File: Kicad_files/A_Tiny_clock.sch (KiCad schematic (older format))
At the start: 29 parts, among them J1 Conn_01x03_Male, J2 USB_B, Q1 Q_NPN_CBE, Q2 Q_NPN_CBE, SW1 SW_MEC_5E, SW2 SW_MEC_5E, SW3 SW_MEC_5E, SW4 SW_MEC_5E, SW5 SW_MEC_5E, U1 ATtiny13A-PU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

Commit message: Updated schematic
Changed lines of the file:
@@
 Text GLabel 6150 3650 2    50   Input ~ 0
 CLOCK_PIN
-$Comp
-L 74xx:74HC595 U3
-U 1 1 61E666FC
-P 8400 5450
-F 0 "U3" H 8400 4569 50  0000 C CNN
-F 1 "74HC595" H 8400 4660 50  0000 C CNN
-F 2 "" H 8400 5450 50  0001 C CNN
-F 3 "http://www.ti.com/lit/ds/symlink/sn74hc595.pdf" H 8400 5450 50  0001 C CNN
-	1    8400 5450
-	1    0    0    1
-$EndComp
 Text GLabel 8000 5850 0    50   Input ~ 0
 DATA_PIN
@@
 	1    7950 5250
 	0    1    1    0
-$EndComp
-Wire Wire Line
-	8800 4300 8000 4300
-Wire Wire Line
-	8000 4300 8000 4000
-$Comp
-L power:VCC #PWR0110
-U 1 1 61E6D320
-P 8400 6200
-F 0 "#PWR0110" H 8400 6050 50  0001 C CNN
-F 1 "VCC" H 8415 6373 50  0000 C CNN
-F 2 "" H 8400 6200 50  0001 C CNN
-F 3 "" H 8400 6200 50  0001 C CNN
-	1    8400 6200
-	-1   0    0    1
-$EndComp
-$Comp
-L power:VCC #PWR0111
-U 1 1 61E6D739
-P 8550 4200
-F 0 "#PWR0111" H 8550 4050 50  0001 C CNN
-F 1 "VCC" H 8565 4373 50  0000 C CNN
-F 2 "" H 8550 4200 50  0001 C CNN
-F 3 "" H 8550 4200 50  0001 C CNN
-	1    8550 4200
-	1    0    0    -1
 $EndComp
 $Comp
@@
 Text GLabel 8800 3800 2    50   Input ~ 0
 Dots
-$Comp
-L power:GND #PWR0116
-U 1 1 61EF6FD2
-P 8700 4750
-F 0 "#PWR0116" H 8700 4500 50  0001 C CNN
-F 1 "GND" H 8705 4577 50  0000 C CNN
-F 2 "" H 8700 4750 50  0001 C CNN
-F 3 "" H 8700 4750 50  0001 C CNN
-	1    8700 4750
-	-1   0    0    1
-$EndComp
 Wire Notes Line
 	4800 5250 500  5250
@@
 Wire Wire Line
 	5550 2900 5550 2950
-Wire Wire Line
-	8700 4750 8400 4750
-Wire Wire Line
-	8800 4300 8800 4950
+$Comp
+L power:GND #PWR0115
+U 1 1 61EF67DF
+P 8750 2750
+F 0 "#PWR0115" H 8750 2500 50  0001 C CNN
+F 1 "GND" H 8755 2577 50  0000 C CNN
+F 2 "" H 8750 2750 50  0001 C CNN
+F 3 "" H 8750 2750 50  0001 C CNN
+	1    8750 2750
+	1    0    0    -1
+$EndComp
+Wire Wire Line
+	8750 2750 8400 2900
+$Comp
+L Connector:Conn_01x03_Male J1
+U 1 1 6224BC17
+P 5700 2000
+F 0 "J1" H 5672 1932 50  0000 R CNN
+F 1 "Conn_01x03_Male" H 5672 2023 50  0000 R CNN
+F 2 "" H 5700 2000 50  0001 C CNN
+F 3 "~" H 5700 2000 50  0001 C CNN
+	1    5700 2000
+	-1   0    0    1
+$EndComp
+Text GLabel 5500 1900 0    50   Input ~ 0
+Clock_VCC
+Text GLabel 5500 2100 0    50   Input ~ 0
+Clock_GND
+Text GLabel 5500 2000 0    50   Input ~ 0
+Clock_Output
+Wire Wire Line
+	5550 4200 5550 4150
+$Comp
+L Connector:USB_B J2
+U 1 1 6226EF95
+P 2750 3800
+F 0 "J2" H 2807 4267 50  0000 C CNN
+F 1 "USB_B" H 2807 4176 50  0000 C CNN
+F 2 "" H 2900 3750 50  0001 C CNN
+F 3 " ~" H 2900 3750 50  0001 C CNN
+	1    2750 3800
+	1    0    0    -1
+$EndComp
+NoConn ~ 3050 3800
+NoConn ~ 3050 3900
+NoConn ~ 2650 4200
+$Comp
+L power:GND #PWR0117
+U 1 1 622821E8
+P 2750 4200
+F 0 "#PWR0117" H 2750 3950 50  0001 C CNN
+F 1 "GND" H 2755 4027 50  0000 C CNN
+F 2 "" H 2750 4200 50  0001 C CNN
+F 3 "" H 2750 4200 50  0001 C CNN
+	1    2750 4200
+	1    0    0    -1
+$EndComp
+$Comp
+L power:VCC #PWR0118
+U 1 1 62282B47
+P 3050 3600
+F 0 "#PWR0118" H 3050 3450 50  0001 C CNN
+F 1 "VCC" H 3065 3773 50  0000 C CNN
+F 2 "" H 3050 3600 50  0001 C CNN
+F 3 "" H 3050 3600 50  0001 C CNN
+	1    3050 3600
+	1    0    0    -1
+$EndComp
+Text Notes 700  3200 0    50   ~ 0
+I soldered wire (with male USB A plug on the other side of wire) directly to board.  \nHere on shcematic i power input is represented by USB B conector but it can be any 5V power supply.
+Wire Notes Line
+	650  4400 4400 4400
+Wire Notes Line
+	4400 4400 4400 3250
+Wire Notes Line
+	4400 3250 4800 3250
+Wire Notes Line
+	4800 3250 4800 3000
+Wire Notes Line
+	4800 3000 650  3000
+Wire Notes Line
+	650  3000 650  4400
+Connection ~ 9950 5950
+Wire Notes Line
+	7100 550  7100 3200
+Wire Notes Line
+	7100 3200 7500 3200
+Wire Notes Line
+	7500 3200 7500 3650
+Wire Notes Line
+	7500 3650 7100 3650
+Wire Notes Line
+	7100 3650 7100 6500
+$Comp
+L power:GND #PWR0116
+U 1 1 61EF6FD2
+P 8950 4750
+F 0 "#PWR0116" H 8950 4500 50  0001 C CNN
+F 1 "GND" H 8955 4577 50  0000 C CNN
+F 2 "" H 8950 4750 50  0001 C CNN
+F 3 "" H 8950 4750 50  0001 C CNN
+	1    8950 4750
+	1    0    0    -1
+$EndComp
+Wire Wire Line
+	8950 4750 8400 4750
+$Comp
+L power:VCC #PWR0110
+U 1 1 61E6D320
+P 8650 6200
+F 0 "#PWR0110" H 8650 6050 50  0001 C CNN
+F 1 "VCC" H 8665 6373 50  0000 C CNN
+F 2 "" H 8650 6200 50  0001 C CNN
+F 3 "" H 8650 6200 50  0001 C CNN
+	1    8650 6200
+	1    0    0    -1
+$EndComp
+$Comp
+L 74xx:74HC595 U3
+U 1 1 61E666FC
+P 8400 5450
+F 0 "U3" H 8400 4569 50  0000 C CNN
+F 1 "74HC595" H 8400 4660 50  0000 C CNN
+F 2 "" H 8400 5450 50  0001 C CNN
+F 3 "http://www.ti.com/lit/ds/symlink/sn74hc595.pdf" H 8400 5450 50  0001 C CNN
+	1    8400 5450
+	1    0    0    1
+$EndComp
+Wire Wire Line
+	8650 6200 8400 6200
 Wire Wire Line
 	8400 6200 8400 6050
-Wire Wire Line
-	8550 4200 8400 4200
+$Comp
+L power:VCC #PWR0111
+U 1 1 61E6D739
+P 8650 4350
+F 0 "#PWR0111" H 8650 4200 50  0001 C CNN
+F 1 "VCC" H 8665 4523 50  0000 C CNN
+F 2 "" H 8650 4350 50  0001 C CNN
+F 3 "" H 8650 4350 50  0001 C CNN
+	1    8650 4350
+	1    0    0    -1
+$EndComp
 $Comp
 L 74xx:74HC595 U2
@@
 	1    0    0    1
 $EndComp
-$Comp
-L power:GND #PWR0115
-U 1 1 61EF67DF
-P 8750 2750
-F 0 "#PWR0115" H 8750 2500 50  0001 C CNN
-F 1 "GND" H 8755 2577 50  0000 C CNN
-F 2 "" H 8750 2750 50  0001 C CNN
-F 3 "" H 8750 2750 50  0001 C CNN
-	1    8750 2750
-	1    0    0    -1
-$EndComp
-Wire Wire Line
-	8750 2750 8400 2900
-$Comp
-L Connector:Conn_01x03_Male J1
-U 1 1 6224BC17
-P 5700 2000
-F 0 "J1" H 5672 1932 50  0000 R CNN
-F 1 "Conn_01x03_Male" H 5672 2023 50  0000 R CNN
-F 2 "" H 5700 2000 50  0001 C CNN
-F 3 "~" H 5700 2000 50  0001 C CNN
-	1    5700 2000
-	-1   0    0    1
-$EndComp
-Text GLabel 5500 1900 0    50   Input ~ 0
-Clock_VCC
-Text GLabel 5500 2100 0    50   Input ~ 0
-Clock_GND
-Text GLabel 5500 2000 0    50   Input ~ 0
-Clock_Output
-Wire Wire Line
-	5550 4200 5550 4150
-$Comp
-L Connector:USB_B J2
-U 1 1 6226EF95
-P 2750 3800
-F 0 "J2" H 2807 4267 50  0000 C CNN
-F 1 "USB_B" H 2807 4176 50  0000 C CNN
-F 2 "" H 2900 3750 50  0001 C CNN
-F 3 " ~" H 2900 3750 50  0001 C CNN
-	1    2750 3800
-	1    0    0    -1
-$EndComp
-NoConn ~ 3050 3800
-NoConn ~ 3050 3900
-NoConn ~ 2650 4200
-$Comp
-L power:GND #PWR0117
-U 1 1 622821E8
-P 2750 4200
-F 0 "#PWR0117" H 2750 3950 50  0001 C CNN
-F 1 "GND" H 2755 4027 50  0000 C CNN
-F 2 "" H 2750 4200 50  0001 C CNN
-F 3 "" H 2750 4200 50  0001 C CNN
-	1    2750 4200
-	1    0    0    -1
-$EndComp
-$Comp
-L power:VCC #PWR0118
-U 1 1 62282B47
-P 3050 3600
-F 0 "#PWR0118" H 3050 3450 50  0001 C CNN
-F 1 "VCC" H 3065 3773 50  0000 C CNN
-F 2 "" H 3050 3600 50  0001 C CNN
-F 3 "" H 3050 3600 50  0001 C CNN
-	1    3050 3600
-	1    0    0    -1
-$EndComp
-Text Notes 700  3200 0    50   ~ 0
-I soldered wire (with male USB A plug on the other side of wire) directly to board.  \nHere on shcematic i power input is represented by USB B conector but it can be any 5V power supply.
-Wire Notes Line
-	650  4400 4400 4400
-Wire Notes Line
-	4400 4400 4400 3250
-Wire Notes Line
-	4400 3250 4800 3250
-Wire Notes Line
-	4800 3250 4800 3000
-Wire Notes Line
-	4800 3000 650  3000
-Wire Notes Line
-	650  3000 650  4400
-Connection ~ 9950 5950
-Wire Notes Line
-	7100 550  7100 3200
-Wire Notes Line
-	7100 3200 7500 3200
-Wire Notes Line
-	7500 3200 7500 3650
-Wire Notes Line
-	7500 3650 7100 3650
-Wire Notes Line
-	7100 3650 7100 6500
+Wire Wire Line
+	8650 4350 8400 4350
+Wire Wire Line
+	8400 4350 8400 4200
+Wire Wire Line
+	8800 4950 8800 4500
+Wire Wire Line
+	8800 4500 8000 4500
+Wire Wire Line
+	8000 4000 8000 4500
 Wire Bus Line
 	9950 5950 9950 6150

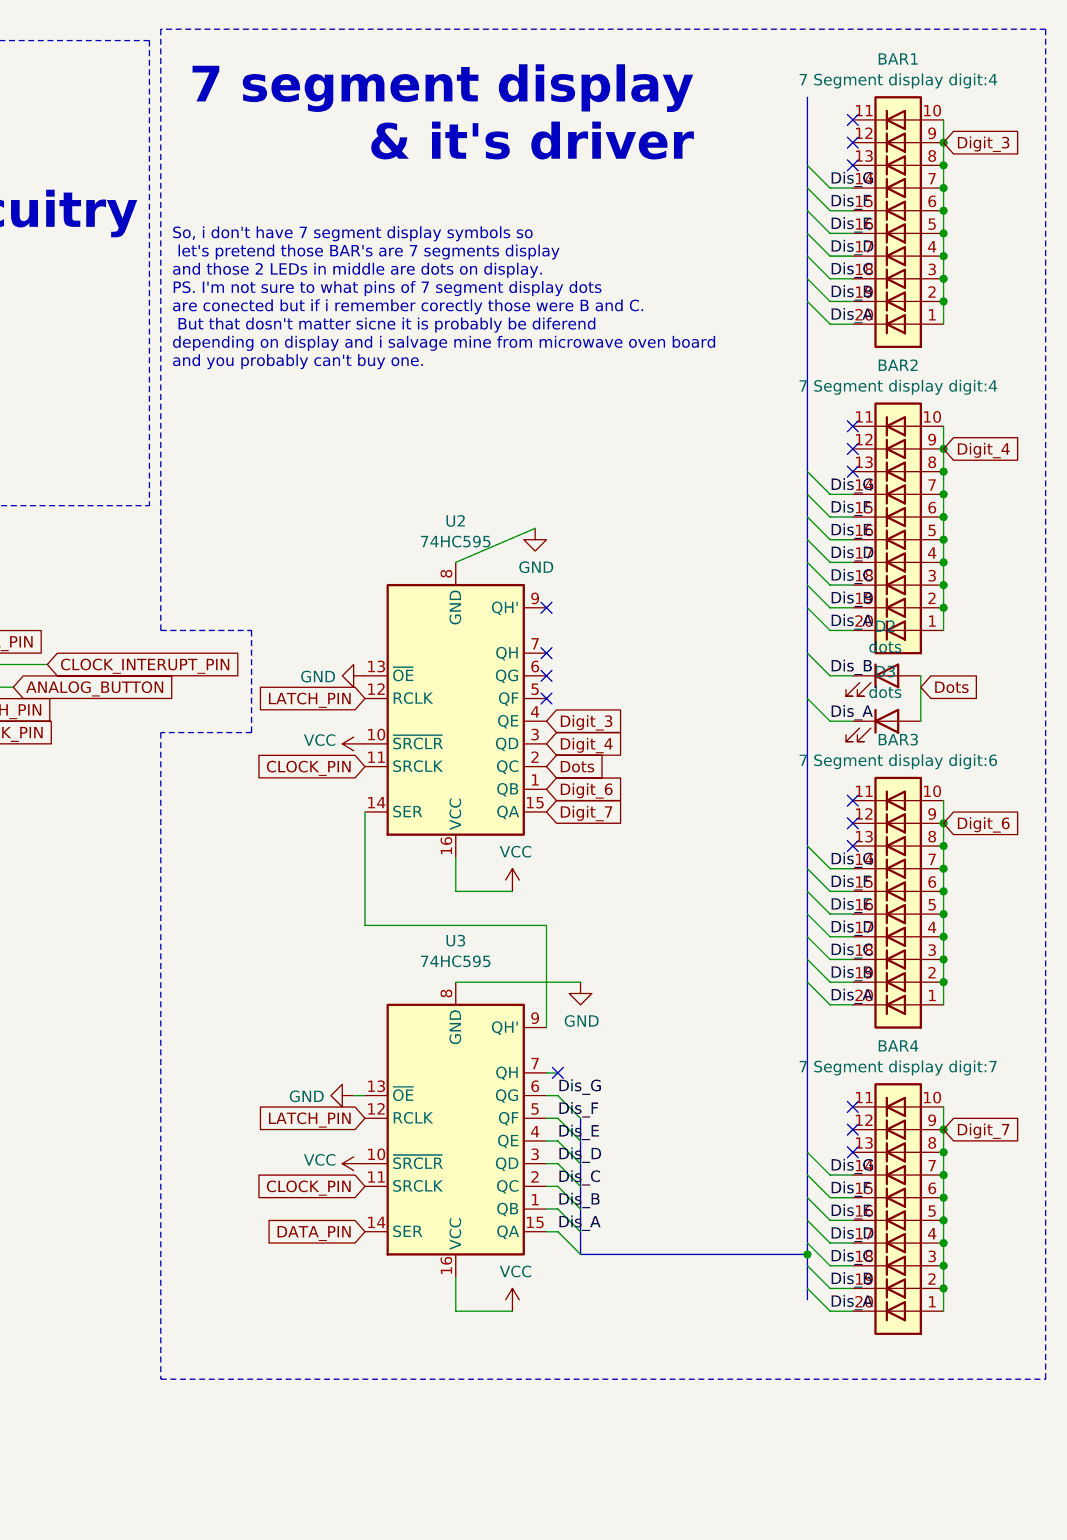
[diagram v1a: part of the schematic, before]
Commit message: Added resistors in 7 seg dis section and claryfications
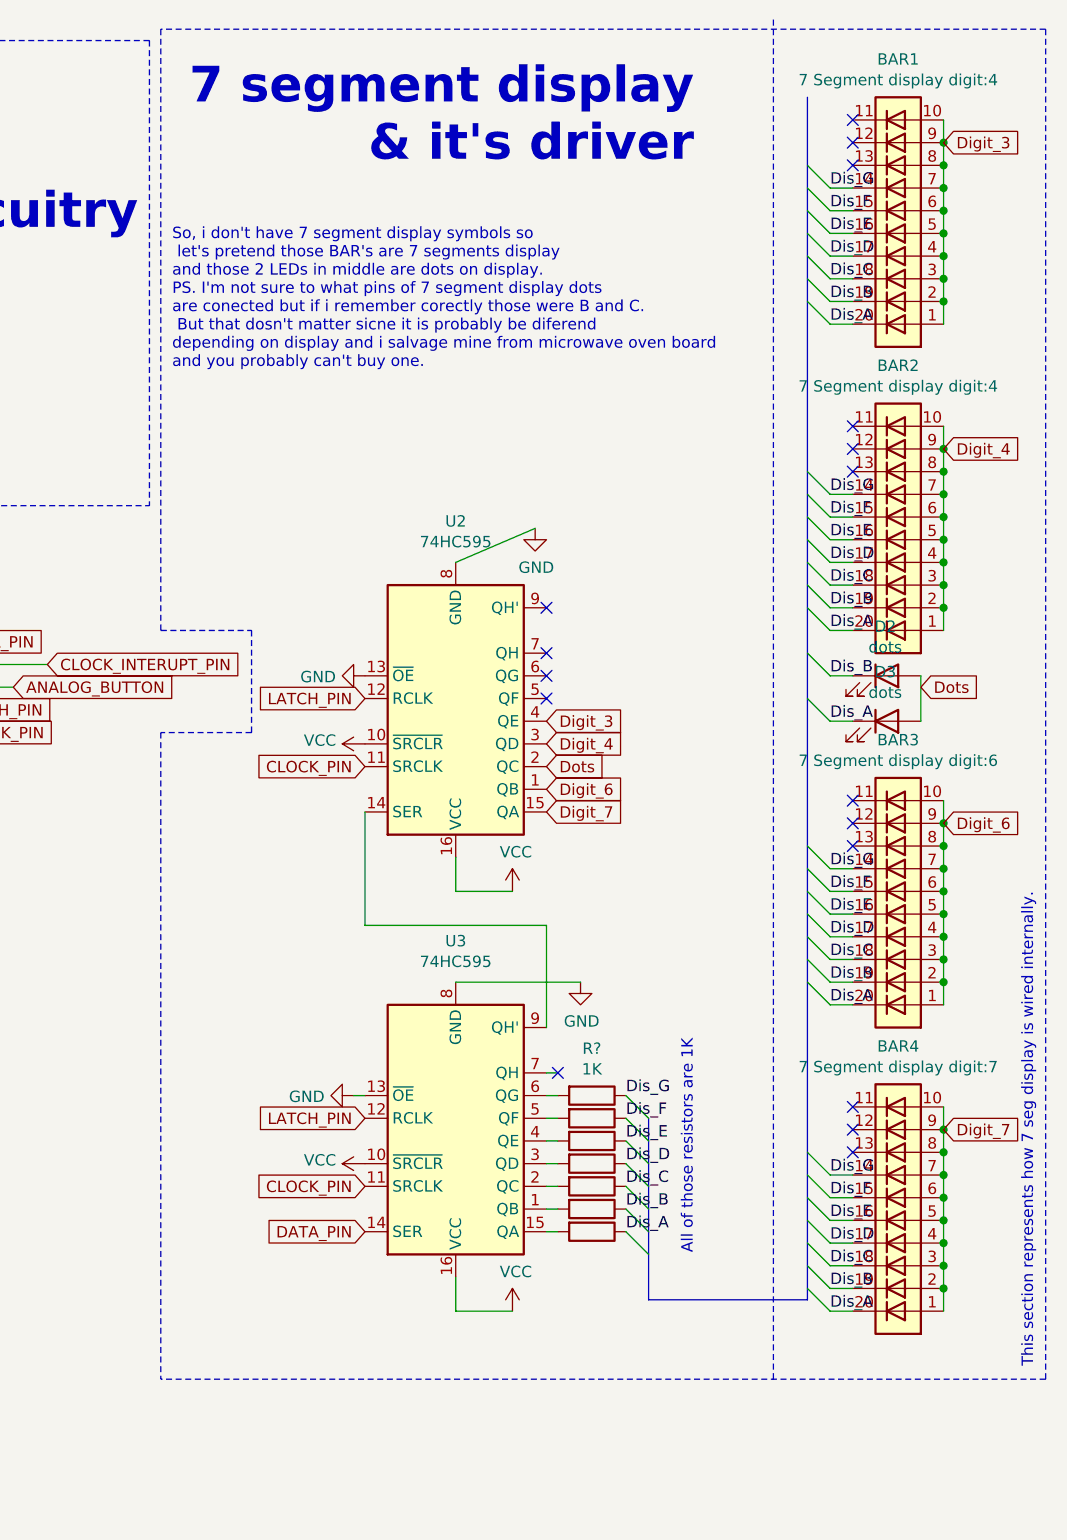
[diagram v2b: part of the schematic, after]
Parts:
- added R? (x7): 1K, symbol Device:R
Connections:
- net Dis_A: now also R?.1; no longer U3.15 (QA)
- net Dis_B: now also R?.1; no longer U3.1 (QB)
- net Dis_C: now also R?.1; no longer U3.2 (QC)
- net Dis_D: now also R?.1; no longer U3.3 (QD)
- net Dis_E: now also R?.1; no longer U3.4 (QE)
- net Dis_F: now also R?.1; no longer U3.5 (QF)
- net Dis_G: now also R?.1; no longer U3.6 (QG)
- new net: R?.2, U3.1 (QB)
- new net: R?.2, U3.15 (QA)
- new net: R?.2, U3.2 (QC)
- new net: R?.2, U3.3 (QD)
- new net: R?.2, U3.4 (QE)
- new net: R?.2, U3.5 (QF)
- new net: R?.2, U3.6 (QG)
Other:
- note added: "All of those resistors are 1K\n"
- note added: "This section represents how 7 seg display is wired internally."
